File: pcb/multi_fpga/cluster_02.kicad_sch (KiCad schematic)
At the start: 7 parts, among them J5 Cluster2_SpokeBus, J6 Cluster2_Power

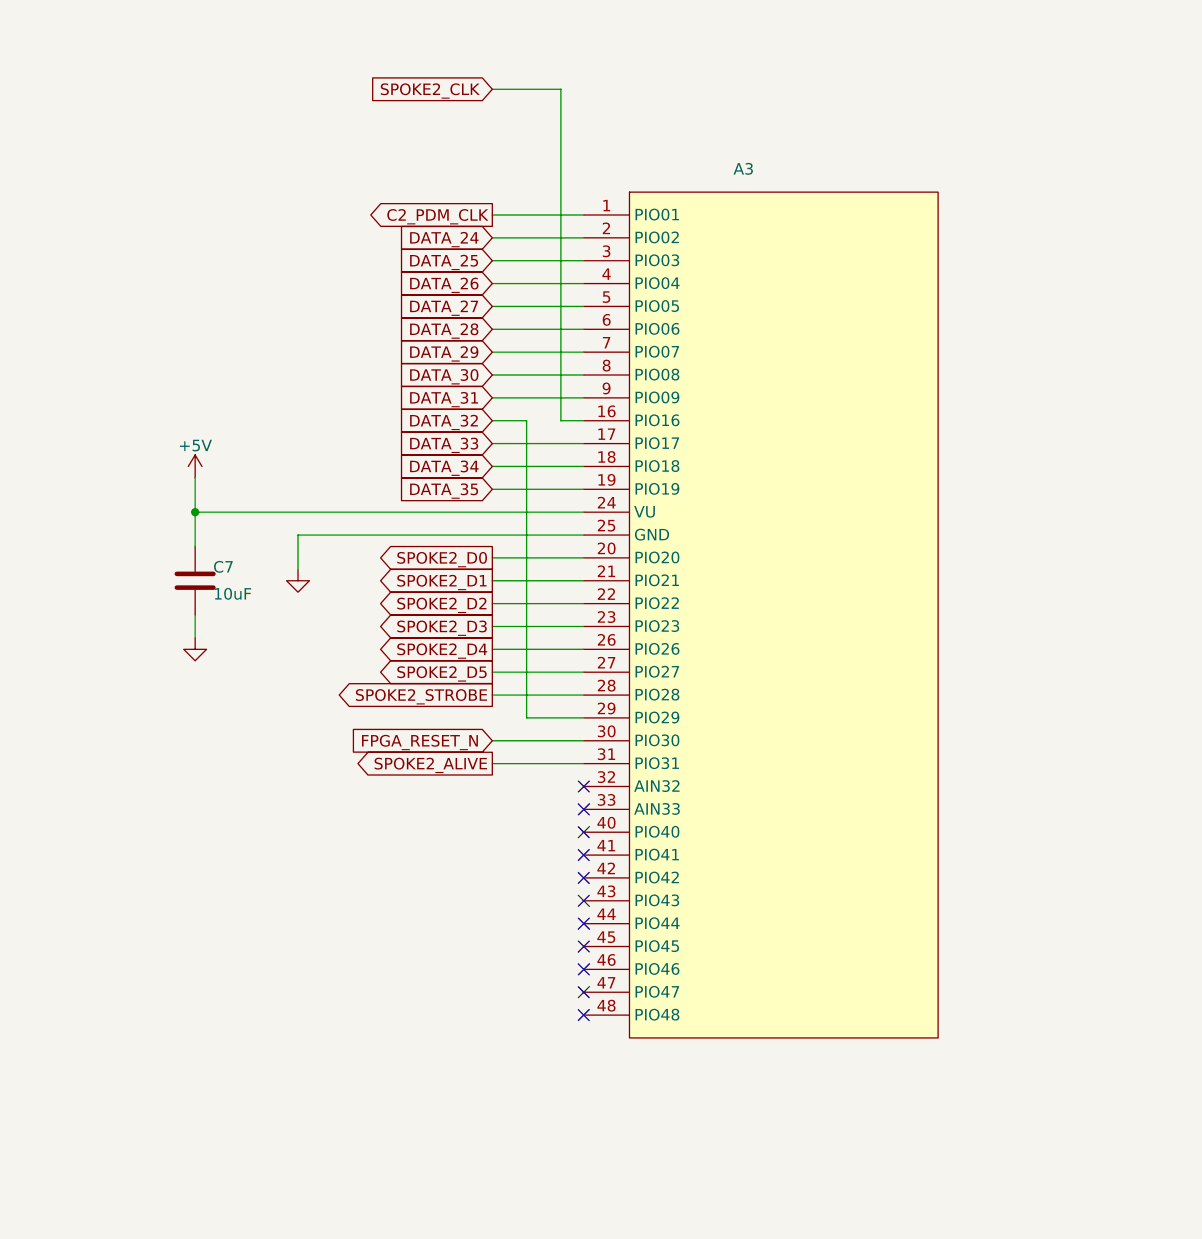
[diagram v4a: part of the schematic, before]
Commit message: Changed CMOD-S7 to CMOD-A7 to fit design.
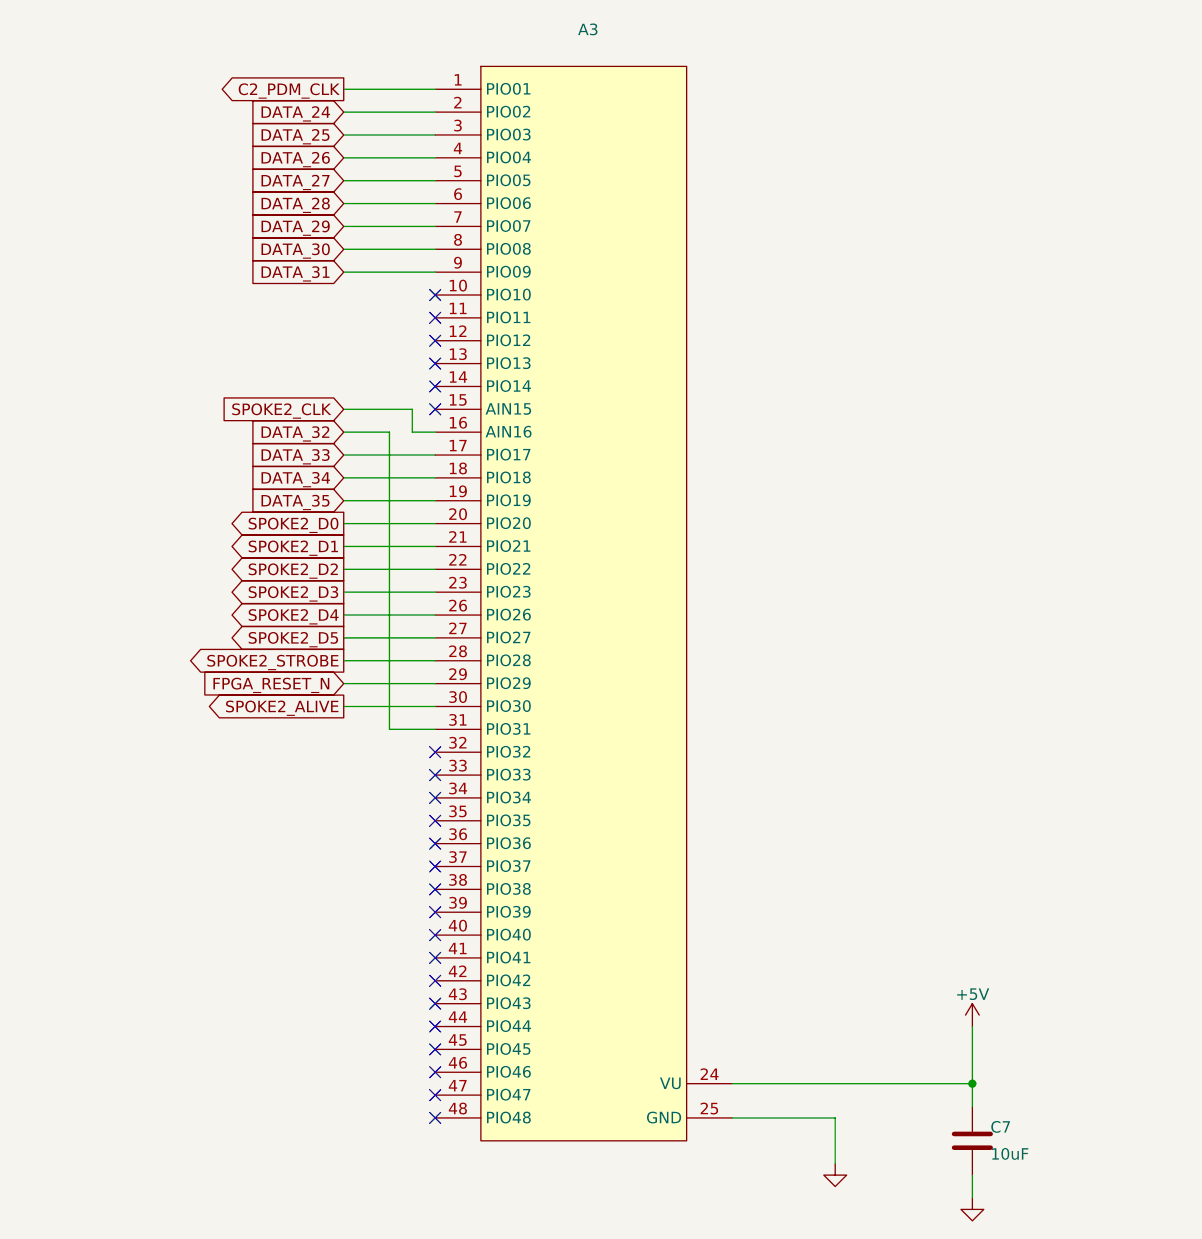
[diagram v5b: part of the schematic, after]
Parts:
- removed A3: (no value), Package_DIP:DIP-48_W15.24mm_Socket, symbol multi_fpga:CMOD_S7
- added A3: (no value), Package_DIP:DIP-48_W15.24mm_Socket, symbol multi_fpga:CMOD_A7_35T
- C7: PROD_ID CAP-13210 -> CAP-24990; Voltage 6.3V -> 10V
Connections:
- net +5V: now also A3.24 (VU)
- net C2_PDM_CLK: now also A3.1 (PIO01)
- net DATA_24: now also A3.2 (PIO02)
- net DATA_25: now also A3.3 (PIO03)
- net DATA_26: now also A3.4 (PIO04)
- net DATA_27: now also A3.5 (PIO05)
- net DATA_28: now also A3.6 (PIO06)
- net DATA_29: now also A3.7 (PIO07)
- net DATA_30: now also A3.8 (PIO08)
- net DATA_31: now also A3.9 (PIO09)
- net DATA_32: now also A3.31 (PIO31)
- net DATA_33: now also A3.17 (PIO17)
- net DATA_34: now also A3.18 (PIO18)
- net DATA_35: now also A3.19 (PIO19)
- net FPGA_RESET_N: now also A3.29 (PIO29)
- net GND: now also A3.25 (GND)
- net SPOKE2_ALIVE: now also A3.30 (PIO30)
- net SPOKE2_CLK: now also A3.16 (AIN16)
- net SPOKE2_D0: now also A3.20 (PIO20)
- net SPOKE2_D1: now also A3.21 (PIO21)
- net SPOKE2_D2: now also A3.22 (PIO22)
- net SPOKE2_D3: now also A3.23 (PIO23)
- net SPOKE2_D4: now also A3.26 (PIO26)
- net SPOKE2_D5: now also A3.27 (PIO27)
- net SPOKE2_STROBE: now also A3.28 (PIO28)
- no-connect marks 11 -> 23

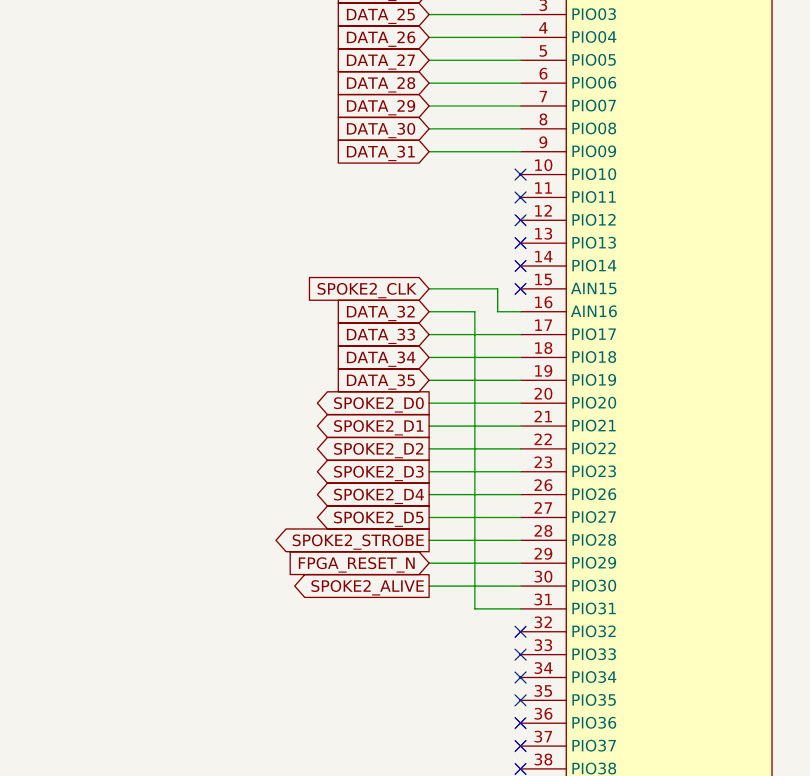
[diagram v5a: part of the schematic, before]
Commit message: Swapped to proper clock pin.
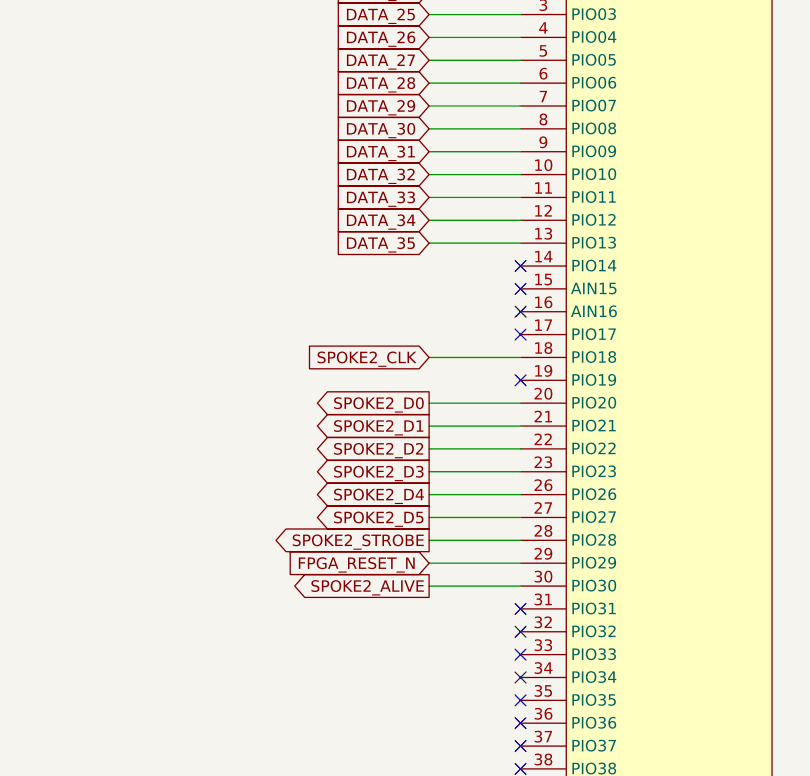
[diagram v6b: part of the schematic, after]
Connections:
- net DATA_32: now also A3.10 (PIO10); no longer A3.31 (PIO31)
- net DATA_33: now also A3.11 (PIO11); no longer A3.17 (PIO17)
- net DATA_34: now also A3.12 (PIO12); no longer A3.18 (PIO18)
- net DATA_35: now also A3.13 (PIO13); no longer A3.19 (PIO19)
- net SPOKE2_CLK: now also A3.18 (PIO18); no longer A3.16 (AIN16)
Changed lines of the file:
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@@
 	)
 	(no_connect
-		(at 176.53 111.76)
+		(at 176.53 127)
 	)
 	(no_connect
@@
 	)
 	(no_connect
-		(at 176.53 116.84)
-	)
-	(no_connect
 		(at 176.53 124.46)
 	)
@@
 	)
 	(no_connect
+		(at 176.53 134.62)
+	)
+	(no_connect
 		(at 176.53 198.12)
 	)
@@
 	)
 	(no_connect
-		(at 176.53 114.3)
+		(at 176.53 129.54)
 	)
 	(no_connect
@@
 	)
 	(no_connect
-		(at 176.53 119.38)
+		(at 176.53 160.02)
 	)
 	(wire
@@
 	(wire
 		(pts
+			(xy 166.37 114.3) (xy 176.53 114.3)
+		)
+		(stroke
+			(width 0)
+			(type default)
+		)
+	)
+	(wire
+		(pts
 			(xy 351.79 186.69) (xy 354.33 186.69)
 		)
@@
 	(wire
 		(pts
-			(xy 171.45 160.02) (xy 176.53 160.02)
-		)
-		(stroke
-			(width 0)
-			(type default)
-		)
-	)
-	(wire
-		(pts
 			(xy 176.53 96.52) (xy 166.37 96.52)
 		)
@@
 	(wire
 		(pts
-			(xy 173.99 127) (xy 176.53 127)
-		)
-		(stroke
-			(width 0)
-			(type default)
-		)
-	)
-	(wire
-		(pts
 			(xy 283.21 186.69) (xy 294.64 186.69)
 		)
@@
 	(wire
 		(pts
-			(xy 173.99 124.46) (xy 166.37 124.46)
-		)
-		(stroke
-			(width 0)
-			(type default)
-		)
-	)
-	(wire
-		(pts
 			(xy 176.53 106.68) (xy 166.37 106.68)
 		)
@@
 	(wire
 		(pts
+			(xy 166.37 119.38) (xy 176.53 119.38)
+		)
+		(stroke
+			(width 0)
+			(type default)
+		)
+	)
+	(wire
+		(pts
 			(xy 166.37 147.32) (xy 176.53 147.32)
 		)
@@
 	(wire
 		(pts
-			(xy 171.45 127) (xy 171.45 160.02)
-		)
-		(stroke
-			(width 0)
-			(type default)
-		)
-	)
-	(wire
-		(pts
 			(xy 321.31 195.58) (xy 321.31 196.85)
 		)
@@
 	(wire
 		(pts
-			(xy 166.37 127) (xy 171.45 127)
-		)
-		(stroke
-			(width 0)
-			(type default)
-		)
-	)
-	(wire
-		(pts
-			(xy 166.37 129.54) (xy 176.53 129.54)
-		)
-		(stroke
-			(width 0)
-			(type default)
-		)
-	)
-	(wire
-		(pts
 			(xy 303.53 119.38) (xy 312.42 119.38)
 		)
@@
 	(wire
 		(pts
-			(xy 173.99 124.46) (xy 173.99 127)
-		)
-		(stroke
-			(width 0)
-			(type default)
-		)
-	)
-	(wire
-		(pts
 			(xy 303.53 116.84) (xy 312.42 116.84)
 		)
@@
 	(wire
 		(pts
-			(xy 166.37 134.62) (xy 176.53 134.62)
+			(xy 166.37 111.76) (xy 176.53 111.76)
+		)
+		(stroke
+			(width 0)
+			(type default)
+		)
+	)
+	(wire
+		(pts
+			(xy 166.37 116.84) (xy 176.53 116.84)
 		)
 		(stroke
@@
 	(global_label "DATA_33"
 		(shape input)
-		(at 166.37 129.54 180)
-		(effects
-			(font
-				(size 1.27 1.27)
-			)
-			(justify right)
-		)
-		(property "Intersheetrefs" "${INTERSHEET_REFS}"
-			(at 166.37 129.54 180)
+		(at 166.37 114.3 180)
+		(effects
+			(font
+				(size 1.27 1.27)
+			)
+			(justify right)
+		)
+		(property "Intersheetrefs" "${INTERSHEET_REFS}"
+			(at 166.37 114.3 180)
 			(hide yes)
 			(show_name no)
@@
 	(global_label "DATA_34"
 		(shape input)
-		(at 166.37 132.08 180)
-		(effects
-			(font
-				(size 1.27 1.27)
-			)
-			(justify right)
-		)
-		(property "Intersheetrefs" "${INTERSHEET_REFS}"
-			(at 166.37 132.08 180)
+		(at 166.37 116.84 180)
+		(effects
+			(font
+				(size 1.27 1.27)
+			)
+			(justify right)
+		)
+		(property "Intersheetrefs" "${INTERSHEET_REFS}"
+			(at 166.37 116.84 180)
 			(hide yes)
 			(show_name no)
@@
 	(global_label "DATA_32"
 		(shape input)
-		(at 166.37 127 180)
-		(effects
-			(font
-				(size 1.27 1.27)
-			)
-			(justify right)
-		)
-		(property "Intersheetrefs" "${INTERSHEET_REFS}"
-			(at 166.37 127 180)
+		(at 166.37 111.76 180)
+		(effects
+			(font
+				(size 1.27 1.27)
+			)
+			(justify right)
+		)
+		(property "Intersheetrefs" "${INTERSHEET_REFS}"
+			(at 166.37 111.76 180)
 			(hide yes)
 			(show_name no)
@@
 	(global_label "SPOKE2_CLK"
 		(shape input)
-		(at 166.37 124.46 180)
-		(effects
-			(font
-				(size 1.27 1.27)
-			)
-			(justify right)
-		)
-		(property "Intersheetrefs" "${INTERSHEET_REFS}"
-			(at 166.37 124.46 180)
+		(at 166.37 132.08 180)
+		(effects
+			(font
+				(size 1.27 1.27)
+			)
+			(justify right)
+		)
+		(property "Intersheetrefs" "${INTERSHEET_REFS}"
+			(at 166.37 132.08 180)
 			(hide yes)
 			(show_name no)
@@
 	(global_label "DATA_35"
 		(shape input)
-		(at 166.37 134.62 180)
-		(effects
-			(font
-				(size 1.27 1.27)
-			)
-			(justify right)
-		)
-		(property "Intersheetrefs" "${INTERSHEET_REFS}"
-			(at 166.37 134.62 180)
-			(hide yes)
-			(show_name no)
+		(at 166.37 119.38 180)
+		(effects
+			(font
+				(size 1.27 1.27)
+			)
+			(justify right)
+		)
+		(property "Intersheetrefs" "${INTERSHEET_REFS}"
+			(at 166.37 119.38 180)
+			(hide yes)
+			(show_name no)

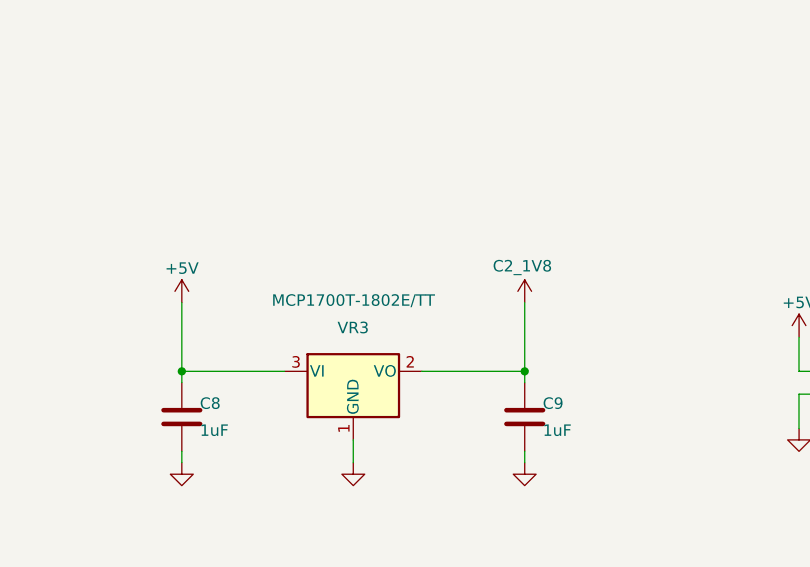
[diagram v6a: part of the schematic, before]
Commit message: Changed mic signals and LDOs to 3V3.
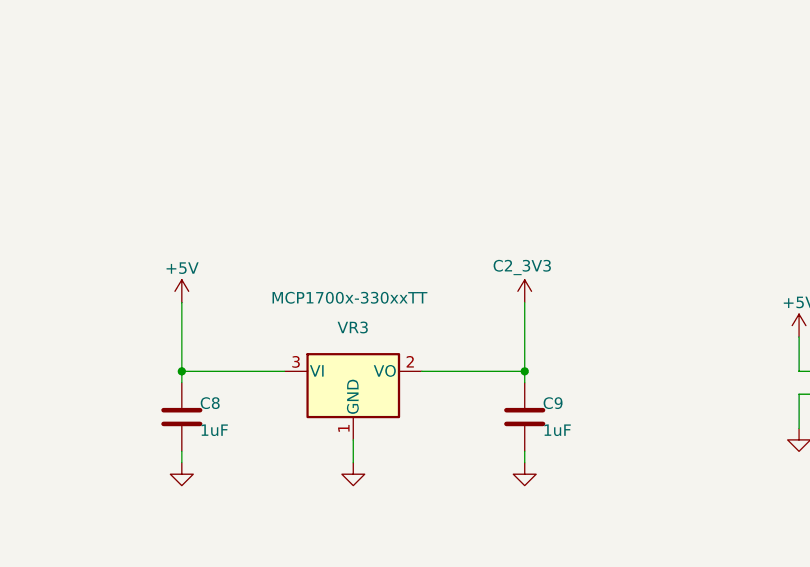
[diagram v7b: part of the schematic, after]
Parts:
- VR3: value MCP1700T-1802E/TT -> MCP1700x-330xxTT; symbol Regulator_Linear:MCP1700x-180xxTT -> Regulator_Linear:MCP1700x-330xxTT
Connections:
- net C2_1V8 renamed C2_3V3
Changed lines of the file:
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@@
 	)
 	(symbol
-		(lib_id "multi_fpga:C2_1V8")
+		(lib_id "multi_fpga:C2_3V3")
 		(at 321.31 179.07 0)
 		(unit 1)
@@
 			)
 		)
-		(property "Value" "C2_1V8"
+		(property "Value" "C2_3V3"
 			(at 321.056 175.006 0)
 			(show_name no)
@@
 	)
 	(symbol
-		(lib_id "Regulator_Linear:MCP1700x-180xxTT")
+		(lib_id "Regulator_Linear:MCP1700x-330xxTT")
 		(at 302.26 186.69 0)
 		(unit 1)
@@
 			)
 		)
-		(property "Value" "MCP1700T-1802E/TT"
-			(at 302.26 178.816 0)
-			(show_name no)
-			(do_not_autoplace no)
-			(effects
-				(font
-					(size 1.27 1.27)
-				)
+		(property "Value" "MCP1700x-330xxTT"
+			(at 293.116 178.562 0)
+			(show_name no)
+			(do_not_autoplace no)
+			(effects
+				(font
+					(size 1.27 1.27)
+				)
+				(justify left)
 			)
 		)
 		(property "Footprint" "Package_TO_SOT_SMD:SOT-23"
+			(at 302.26 180.975 0)
+			(hide yes)
+			(show_name no)
+			(do_not_autoplace no)
+			(effects
+				(font
+					(size 1.27 1.27)
+				)
+			)
+		)
+		(property "Datasheet" "http://ww1.microchip.com/downloads/en/DeviceDoc/20001826D.pdf"
 			(at 302.26 186.69 0)
 			(hide yes)
@@
 			)
 		)
-		(property "Datasheet" ""
+		(property "Description" "250mA Low Quiscent Current LDO, 3.3V output, SOT-23"
 			(at 302.26 186.69 0)
 			(hide yes)
-			(show_name no)
-			(do_not_autoplace no)
-			(effects
-				(font
-					(size 1.27 1.27)
-				)
-			)
-		)
-		(property "Description" ""
-			(at 302.26 186.69 0)
-			(hide yes)

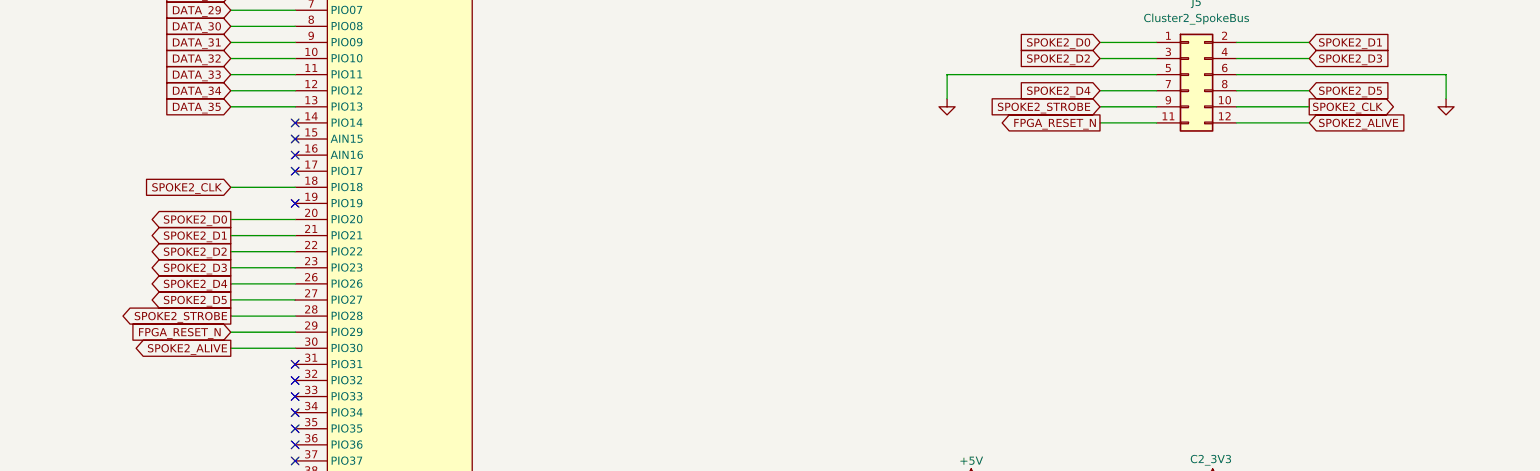
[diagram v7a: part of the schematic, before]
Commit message: Changed from per-spoke to shared spoke alive signals.
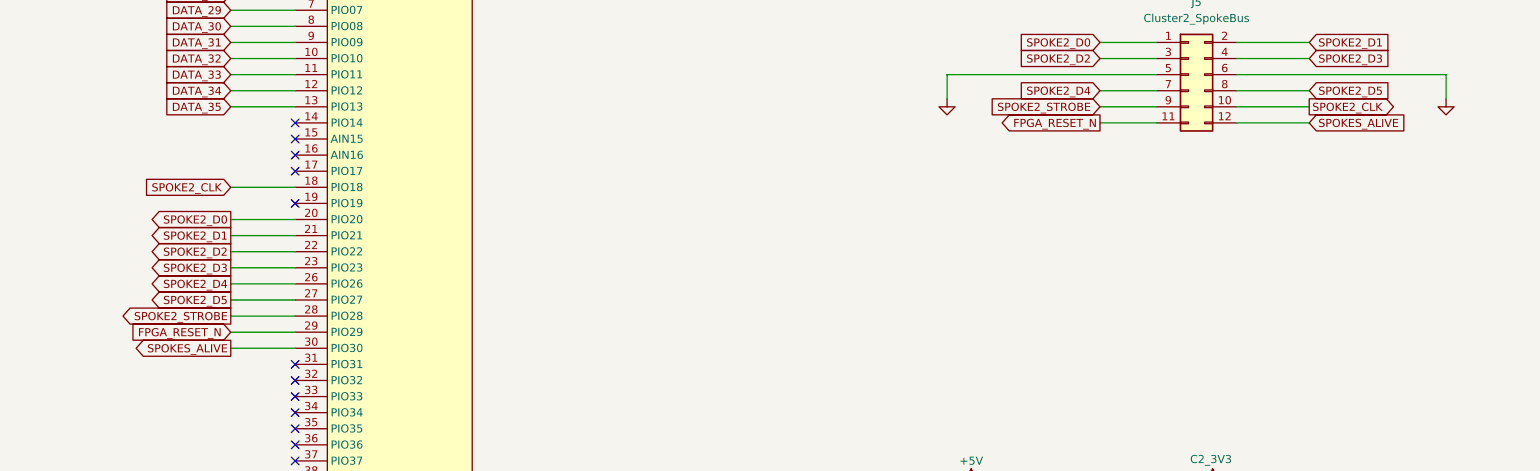
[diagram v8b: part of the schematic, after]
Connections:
- net SPOKE2_ALIVE renamed SPOKES_ALIVE
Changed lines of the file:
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@@
 		)
 	)
-	(global_label "SPOKE2_ALIVE"
+	(global_label "SPOKES_ALIVE"
 		(shape output)
 		(at 166.37 157.48 180)
@@
 		)
 	)
-	(global_label "SPOKE2_ALIVE"
+	(global_label "SPOKES_ALIVE"
 		(shape input)
 		(at 336.55 121.92 0)
